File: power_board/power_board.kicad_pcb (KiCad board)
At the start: 2 copper layers, 171.8 x 117.7 mm, 88 parts, among them J1 PROG, J10 M4, J11 5V_1, J12 M5, J13 M6, J14 M7, J15 FAN, J16 Screw_Terminal_01x02, J17 MB_interface, J18 Conn_01x02_Female, J19 12V_1, J2 M1, J20 12V_2, J21 12V_3, J22 12V_4, J23 48V_1, J24 48V_2, J25 48V_3, J26 48V_4, J27 Screw_Terminal_01x02, J3 M2, J4 Conn_01x02_Female, J5 Conn_01x02_Female, J6 Conn_01x01_Male, J7 Conn_01x01_Male, J8 Screw_Terminal_01x02, J9 M3, Q1 2N3906, SW1 SW_Push, U1 ACS758xCB-050B-PFF, U10 MAX31855KASA, U2 ACS758xCB-050B-PFF, U3 MCP2515-EST, U4 MAX31855KASA, U5 ATA6560,1, U6 BTS50085-1TMA, U7 ATmega328P-AU, U8 BTS50085-1TMA, U9 LM2596S-5, Y1 20Mhz, Y2 16Mhz

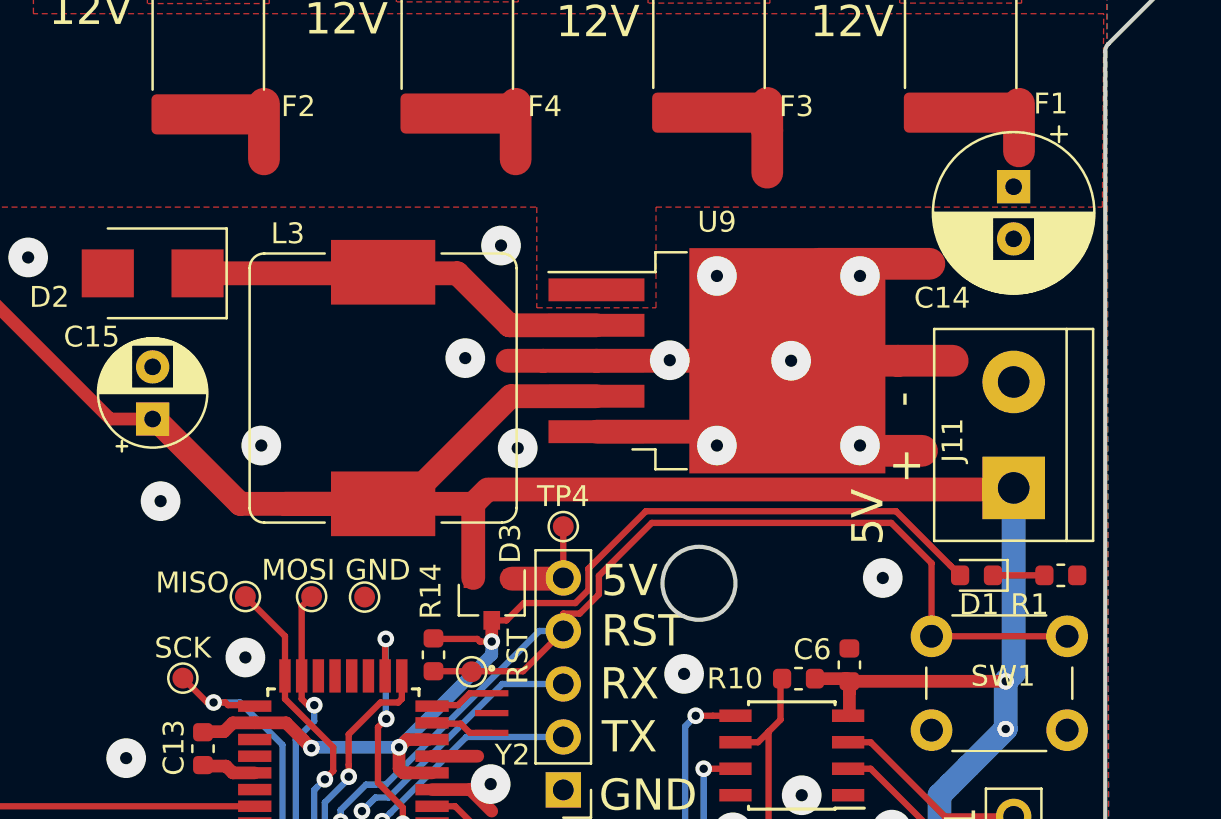
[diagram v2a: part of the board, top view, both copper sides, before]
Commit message: Changed 5v input capacitor package
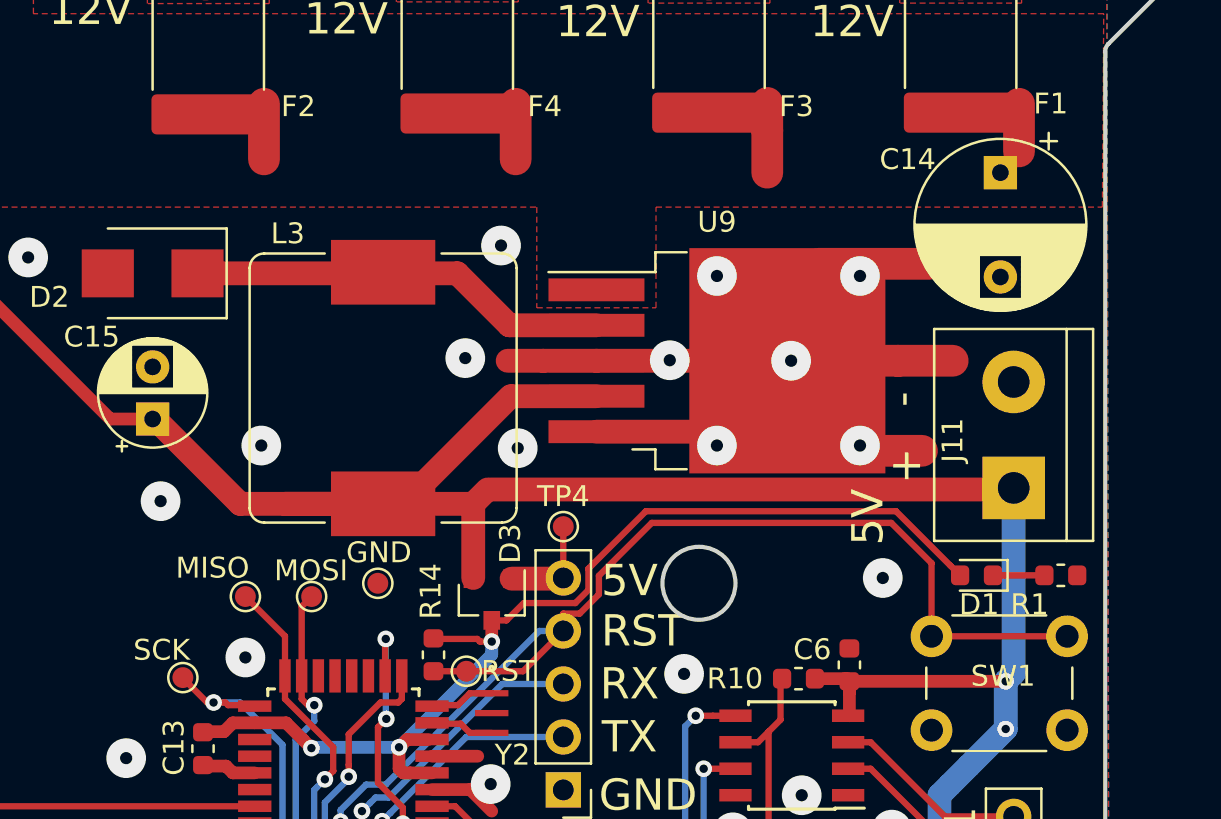
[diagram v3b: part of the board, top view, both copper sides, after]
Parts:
- removed GND: GND, TestPoint:TestPoint_Pad_D1.0mm
- removed MISO: MISO, TestPoint:TestPoint_Pad_D1.0mm
- removed MOSI: MOSI, TestPoint:TestPoint_Pad_D1.0mm
- removed RST: RST, TestPoint:TestPoint_Pad_D1.0mm
- removed SCK: SCK, TestPoint:TestPoint_Pad_D1.0mm
- added TP1: MISO, TestPoint:TestPoint_Pad_D1.0mm, F.Cu at (184.8, 71.8)
- added TP2: SCK, TestPoint:TestPoint_Pad_D1.0mm, F.Cu at (181.8, 75.6)
- added TP3: RST, TestPoint:TestPoint_Pad_D1.0mm, F.Cu at (195.4, 75.3)
- added TP5: MOSI, TestPoint:TestPoint_Pad_D1.0mm, F.Cu at (188.0, 71.8)
- added TP6: GND, TestPoint:TestPoint_Pad_D1.0mm, F.Cu at (191.1, 71.1)
- C14: footprint Capacitor_THT:CP_Radial_D7.5mm_P2.50mm -> Capacitor_THT:CP_Radial_D8.0mm_P5.00mm
- moved C14 0.93 mm to (221.0, 51.4)
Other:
- board text added: "MISO"
- board text added: "MOSI"
- board text added: "SCK"

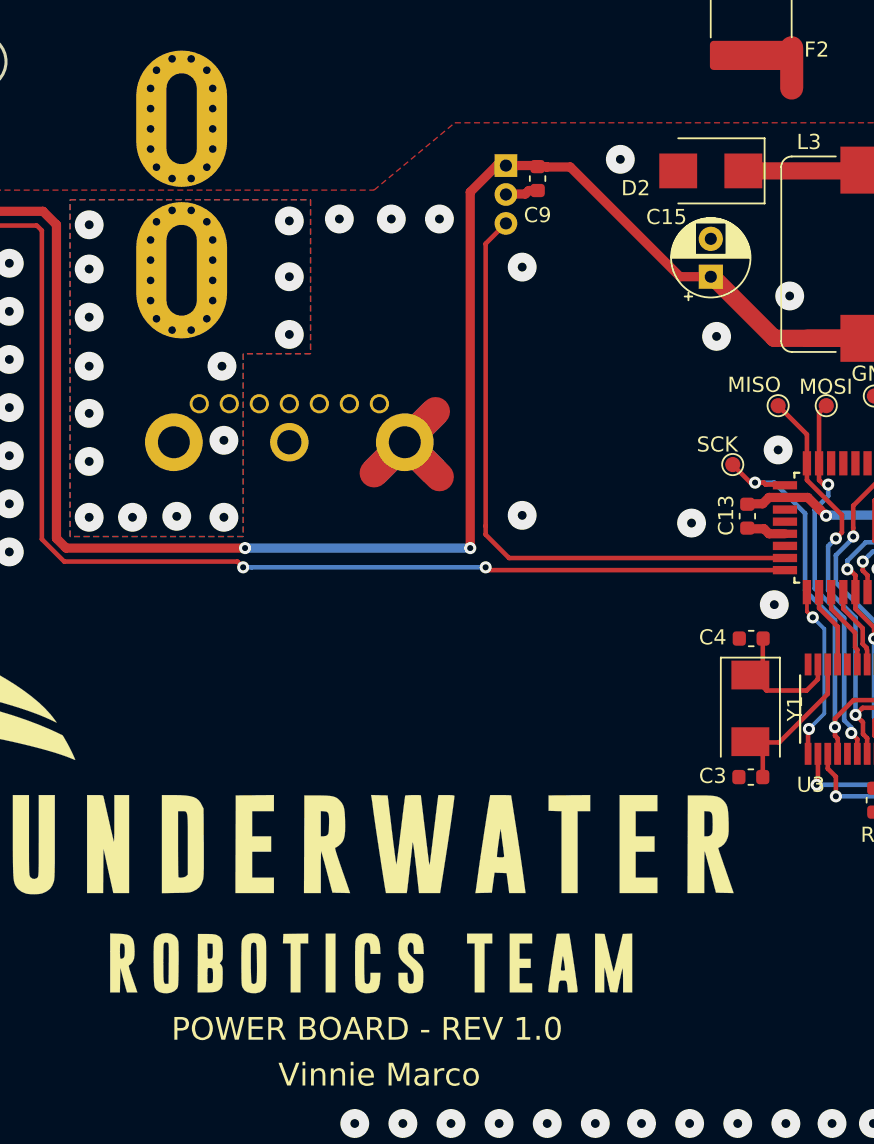
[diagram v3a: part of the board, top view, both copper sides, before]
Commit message: Updated D2 package
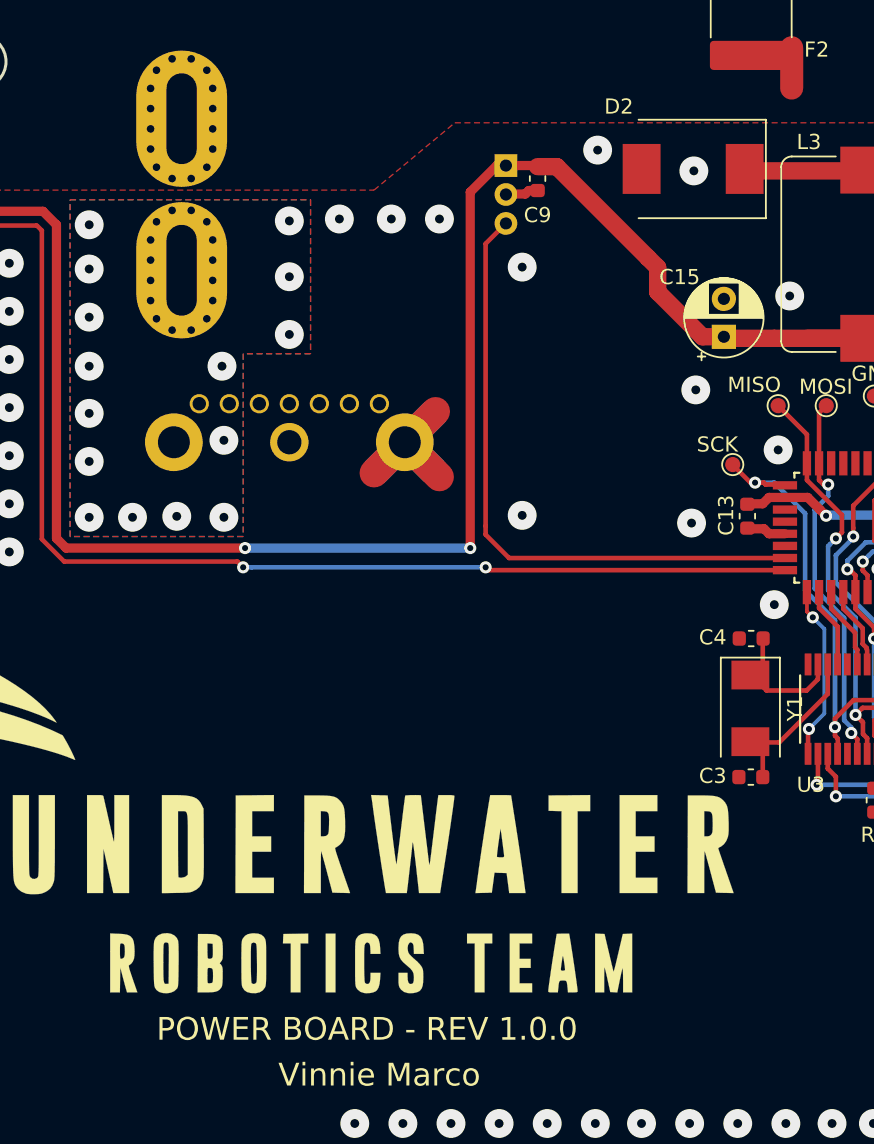
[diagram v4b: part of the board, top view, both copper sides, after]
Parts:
- C14: value 680uF -> 470uF
- D2: footprint Diode_SMD:D_SMB -> Diode_SMD:D_SMC
- moved C15 4.06 mm to (181.2, 67.2)
- moved D2 1.17 mm to (179.2, 56.1)
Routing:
- net +5V: track 272.4 -> 273.3 mm
- net GNDREF: vias 111 -> 112
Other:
- board text added: "POWER BOARD - REV 1.0.0"
- board text removed: "POWER BOARD - REV 1.0"
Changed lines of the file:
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@@
     (thickness 1.6)
     (drawings 84)
-    (tracks 868)
+    (tracks 870)
     (zones 0)
     (modules 88)
@@
   )
   (setup
-    (last_trace_width 0.3048)
+    (last_trace_width 0.6096)
     (user_trace_width 0.3048)
     (user_trace_width 0.6096)
@@
     (add_net V_MCU)
   )
+  (module Diode_SMD:D_SMC (layer F.Cu)
+    (at 179.1752 56.134 180)
+    (descr "Diode SMC (DO-214AB)")
+    (tags "Diode SMC (DO-214AB)")
+    (attr smd)
+    (fp_text reference D2 (at 4.9058 4.1148 180) (layer F.SilkS)
+      (effects (font (size 1 1) (thickness 0.15)))
+    )
+    (fp_text value 1N5824 (at 0 4.2 180) (layer F.Fab)
+      (effects (font (size 1 1) (thickness 0.15)))
+    )
+    (fp_text user %R (at 0 -1.9 180) (layer F.Fab)
+      (effects (font (size 1 1) (thickness 0.15)))
+    )
+    (fp_line (start -4.8 3.25) (end -4.8 -3.25) (layer F.SilkS) (width 0.12))
+    (fp_line (start 3.55 3.1) (end -3.55 3.1) (layer F.Fab) (width 0.1))
+    (fp_line (start -3.55 3.1) (end -3.55 -3.1) (layer F.Fab) (width 0.1))
+    (fp_line (start 3.55 -3.1) (end 3.55 3.1) (layer F.Fab) (width 0.1))
+    (fp_line (start 3.55 -3.1) (end -3.55 -3.1) (layer F.Fab) (width 0.1))
+    (fp_line (start -4.9 -3.35) (end 4.9 -3.35) (layer F.CrtYd) (width 0.05))
+    (fp_line (start 4.9 -3.35) (end 4.9 3.35) (layer F.CrtYd) (width 0.05))
+    (fp_line (start 4.9 3.35) (end -4.9 3.35) (layer F.CrtYd) (width 0.05))
+    (fp_line (start -4.9 3.35) (end -4.9 -3.35) (layer F.CrtYd) (width 0.05))
+    (fp_line (start -0.64944 0.00102) (end -1.55114 0.00102) (layer F.Fab) (width 0.1))
+    (fp_line (start 0.50118 0.00102) (end 1.4994 0.00102) (layer F.Fab) (width 0.1))
+    (fp_line (start -0.64944 -0.79908) (end -0.64944 0.80112) (layer F.Fab) (width 0.1))
+    (fp_line (start 0.50118 0.75032) (end 0.50118 -0.79908) (layer F.Fab) (width 0.1))
+    (fp_line (start -0.64944 0.00102) (end 0.50118 0.75032) (layer F.Fab) (width 0.1))
+    (fp_line (start -0.64944 0.00102) (end 0.50118 -0.79908) (layer F.Fab) (width 0.1))
+    (fp_line (start -4.8 3.25) (end 3.6 3.25) (layer F.SilkS) (width 0.12))
+    (fp_line (start -4.8 -3.25) (end 3.6 -3.25) (layer F.SilkS) (width 0.12))
+    (pad 1 smd rect (at -3.4 0 270) (size 3.3 2.5) (layers F.Cu F.Paste F.Mask)
+      (net 48 "Net-(D2-Pad1)"))
+    (pad 2 smd rect (at 3.4 0 270) (size 3.3 2.5) (layers F.Cu F.Paste F.Mask)
+      (net 5 GNDREF))
+    (model ${KISYS3DMOD}/Diode_SMD.3dshapes/D_SMC.wrl
+      (at (xyz 0 0 0))
+      (scale (xyz 1 1 1))
+      (rotate (xyz 0 0 0))
+    )
+  )
   (module Capacitor_THT:CP_Radial_D8.0mm_P5.00mm (layer F.Cu)
     (at 220.98 51.435 270)
@@
       (effects (font (size 1 1) (thickness 0.15)))
     )
-    (fp_text value 680uF (at 2.5 5.25 270) (layer F.Fab)
+    (fp_text value 470uF (at 2.5 5.25 270) (layer F.Fab)
       (effects (font (size 1 1) (thickness 0.15)))
     )
@@
       (net 24 "Net-(U7-Pad7)"))
   )
-  (module Diode_SMD:D_SMB (layer F.Cu)
-    (at 180.34 56.261 180)
-    (descr "Diode SMB (DO-214AA)")
-    (tags "Diode SMB (DO-214AA)")
-    (attr smd)
-    (fp_text reference D2 (at 4.953 -1.143 180) (layer F.SilkS)
-      (effects (font (size 1 1) (thickness 0.15)))
-    )
-    (fp_text value 1N5824 (at 0 3.1 180) (layer F.Fab)
-      (effects (font (size 1 1) (thickness 0.15)))
-    )
-    (fp_text user %R (at 0 -3 180) (layer F.Fab)
-      (effects (font (size 1 1) (thickness 0.15)))
-    )
-    (fp_line (start -3.55 -2.15) (end -3.55 2.15) (layer F.SilkS) (width 0.12))
-    (fp_line (start 2.3 2) (end -2.3 2) (layer F.Fab) (width 0.1))
-    (fp_line (start -2.3 2) (end -2.3 -2) (layer F.Fab) (width 0.1))
-    (fp_line (start 2.3 -2) (end 2.3 2) (layer F.Fab) (width 0.1))
-    (fp_line (start 2.3 -2) (end -2.3 -2) (layer F.Fab) (width 0.1))
-    (fp_line (start -3.65 -2.25) (end 3.65 -2.25) (layer F.CrtYd) (width 0.05))
-    (fp_line (start 3.65 -2.25) (end 3.65 2.25) (layer F.CrtYd) (width 0.05))
-    (fp_line (start 3.65 2.25) (end -3.65 2.25) (layer F.CrtYd) (width 0.05))
-    (fp_line (start -3.65 2.25) (end -3.65 -2.25) (layer F.CrtYd) (width 0.05))
-    (fp_line (start -0.64944 0.00102) (end -1.55114 0.00102) (layer F.Fab) (width 0.1))
-    (fp_line (start 0.50118 0.00102) (end 1.4994 0.00102) (layer F.Fab) (width 0.1))
-    (fp_line (start -0.64944 -0.79908) (end -0.64944 0.80112) (layer F.Fab) (width 0.1))
-    (fp_line (start 0.50118 0.75032) (end 0.50118 -0.79908) (layer F.Fab) (width 0.1))
-    (fp_line (start -0.64944 0.00102) (end 0.50118 0.75032) (layer F.Fab) (width 0.1))
-    (fp_line (start -0.64944 0.00102) (end 0.50118 -0.79908) (layer F.Fab) (width 0.1))
-    (fp_line (start -3.55 2.15) (end 2.15 2.15) (layer F.SilkS) (width 0.12))
-    (fp_line (start -3.55 -2.15) (end 2.15 -2.15) (layer F.SilkS) (width 0.12))
-    (pad 1 smd rect (at -2.15 0 180) (size 2.5 2.3) (layers F.Cu F.Paste F.Mask)
-      (net 48 "Net-(D2-Pad1)"))
-    (pad 2 smd rect (at 2.15 0 180) (size 2.5 2.3) (layers F.Cu F.Paste F.Mask)
-      (net 5 GNDREF))
-    (model ${KISYS3DMOD}/Diode_SMD.3dshapes/D_SMB.wrl
-      (at (xyz 0 0 0))
-      (scale (xyz 1 1 1))
-      (rotate (xyz 0 0 0))
-    )
-  )
   (module TerminalBlock:TerminalBlock_bornier-2_P5.08mm (layer F.Cu)
     (at 98.425 36.195 180)
@@
   )
   (module Capacitor_THT:CP_Radial_D5.0mm_P2.50mm (layer F.Cu)
-    (at 180.34 63.246 90)
+    (at 181.2036 67.2084 90)
     (descr "CP, Radial series, Radial, pin pitch=2.50mm, , diameter=5mm, Electrolytic Capacitor")
     (tags "CP Radial series Radial pin pitch 2.50mm  diameter 5mm Electrolytic Capacitor")
@@
     (effects (font (size 1.5 1.5) (thickness 0.375)))
   )
-  (gr_text "POWER BOARD - REV 1.0" (at 157.6578 112.903) (layer F.SilkS)
+  (gr_text "POWER BOARD - REV 1.0.0" (at 157.6578 112.903) (layer F.SilkS)
     (effects (font (size 1.5 1.5) (thickness 0.375)))
   )
@@
   (segment (start 197.563 62.152) (end 197.497 62.152) (width 0.25) (layer F.Cu) (net 3))
   (segment (start 192.212 67.437) (end 191.389 67.437) (width 1.143) (layer F.Cu) (net 3))
-  (segment (start 184.531 67.31) (end 180.34 63.119) (width 1.143) (layer F.Cu) (net 3))
   (segment (start 191.389 67.31) (end 184.531 67.31) (width 1.143) (layer F.Cu) (net 3))
-  (segment (start 178.308 63.246) (end 180.34 63.246) (width 0.6096) (layer F.Cu) (net 3))
-  (segment (start 171.069 56.007) (end 178.308 63.246) (width 0.6096) (layer F.Cu) (net 3))
-  (segment (start 169.5105 56.007) (end 171.069 56.007) (width 0.6096) (layer F.Cu) (net 3))
-  (segment (start 168.91 55.9815) (end 169.485 55.9815) (width 0.6096) (layer F.Cu) (net 3))
-  (segment (start 169.485 55.9815) (end 169.5105 56.007) (width 0.6096) (layer F.Cu) (net 3))
   (segment (start 219.456 79.883) (end 218.567 80.772) (width 1.143) (layer B.Cu) (net 3))
   (segment (start 212.782685 96.012) (end 212.217 96.012) (width 1.143) (layer B.Cu) (net 3))
@@
   (segment (start 221.615 75.438) (end 221.234 75.819) (width 1.143) (layer B.Cu) (net 3))
   (via (at 221.234 75.819) (size 0.8) (drill 0.4) (layers F.Cu B.Cu) (net 3))
+  (segment (start 168.91 55.9815) (end 170.1799 55.9815) (width 1.143) (layer F.Cu) (net 3))
+  (segment (start 170.1799 55.9815) (end 176.1998 62.0014) (width 1.143) (layer F.Cu) (net 3))
+  (segment (start 184.531 67.31) (end 181.2036 67.31) (width 1.143) (layer F.Cu) (net 3))
+  (segment (start 179.794 67.2084) (end 176.8348 64.2492) (width 1.143) (layer F.Cu) (net 3))
+  (segment (start 181.2036 67.2084) (end 179.794 67.2084) (width 1.143) (layer F.Cu) (net 3))
+  (segment (start 176.8348 62.6364) (end 176.1998 62.0014) (width 1.143) (layer F.Cu) (net 3))
+  (segment (start 176.8348 64.2492) (end 176.8348 62.6364) (width 1.143) (layer F.Cu) (net 3))
   (segment (start 167.027 81.81) (end 165.481 80.264) (width 0.3048) (layer F.Cu) (net 4))
   (segment (start 185.234 81.81) (end 167.027 81.81) (width 0.3048) (layer F.Cu) (net 4))
@@
   (segment (start 183.857 79.883) (end 182.753 79.883) (width 0.6096) (layer F.Cu) (net 5))
   (via (at 184.785 74.676) (size 1.905) (drill 0.5842) (layers F.Cu B.Cu) (net 5))
-  (via (at 180.721 67.183) (size 1.905) (drill 0.5842) (layers F.Cu B.Cu) (net 5))
+  (via (at 179.3494 70.7136) (size 1.905) (drill 0.5842) (layers F.Cu B.Cu) (net 5))
   (via (at 167.894 78.994) (size 1.905) (drill 0.5842) (layers F.Cu B.Cu) (net 5))
   (segment (start 144.907 124.968) (end 147.193 122.682) (width 1.905) (layer F.Cu) (net 5))
@@
   (segment (start 125.413 57.959) (end 124.286 57.959) (width 0.6096) (layer F.Cu) (net 5))
   (via (at 179.07 79.502) (size 1.905) (drill 0.5842) (layers F.Cu B.Cu) (net 5))
-  (via (at 174.371 55.499) (size 1.905) (drill 0.5842) (layers F.Cu B.Cu) (net 5))
+  (via (at 172.8724 54.8894) (size 1.905) (drill 0.5842) (layers F.Cu B.Cu) (net 5))
   (segment (start 193.734 81.01) (end 195.564 81.01) (width 0.6096) (layer F.Cu) (net 5))
   (segment (start 195.564 81.01) (end 196.596 82.042) (width 0.6096) (layer F.Cu) (net 5))
@@
   (via (at 134.0485 78.232) (size 1.905) (drill 0.5842) (layers F.Cu B.Cu) (net 5))
   (via (at 134.0485 81.407) (size 1.905) (drill 0.5842) (layers F.Cu B.Cu) (net 5))
+  (via (at 179.2224 56.261) (size 1.905) (drill 0.5842) (layers F.Cu B.Cu) (net 5))
   (segment (start 98.425 36.195) (end 98.425 37.945) (width 0.25) (layer F.Cu) (net 6))
   (segment (start 110.49 36.195) (end 110.49 37.945) (width 0.25) (layer F.Cu) (net 6))
